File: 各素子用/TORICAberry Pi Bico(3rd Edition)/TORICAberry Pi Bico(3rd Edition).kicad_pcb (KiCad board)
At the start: 2 copper layers, 24.2 x 33.9 mm, 47 parts, among them J1 USB_C_Receptacle, J2 Conn_01x08_Socket, J5 Conn_01x11_Socket, SW1 SW_Push, SW2 SW_Push, U1 RP2040, U3 NCP1117-3.3_TO252, Y1 Crystal_GND24

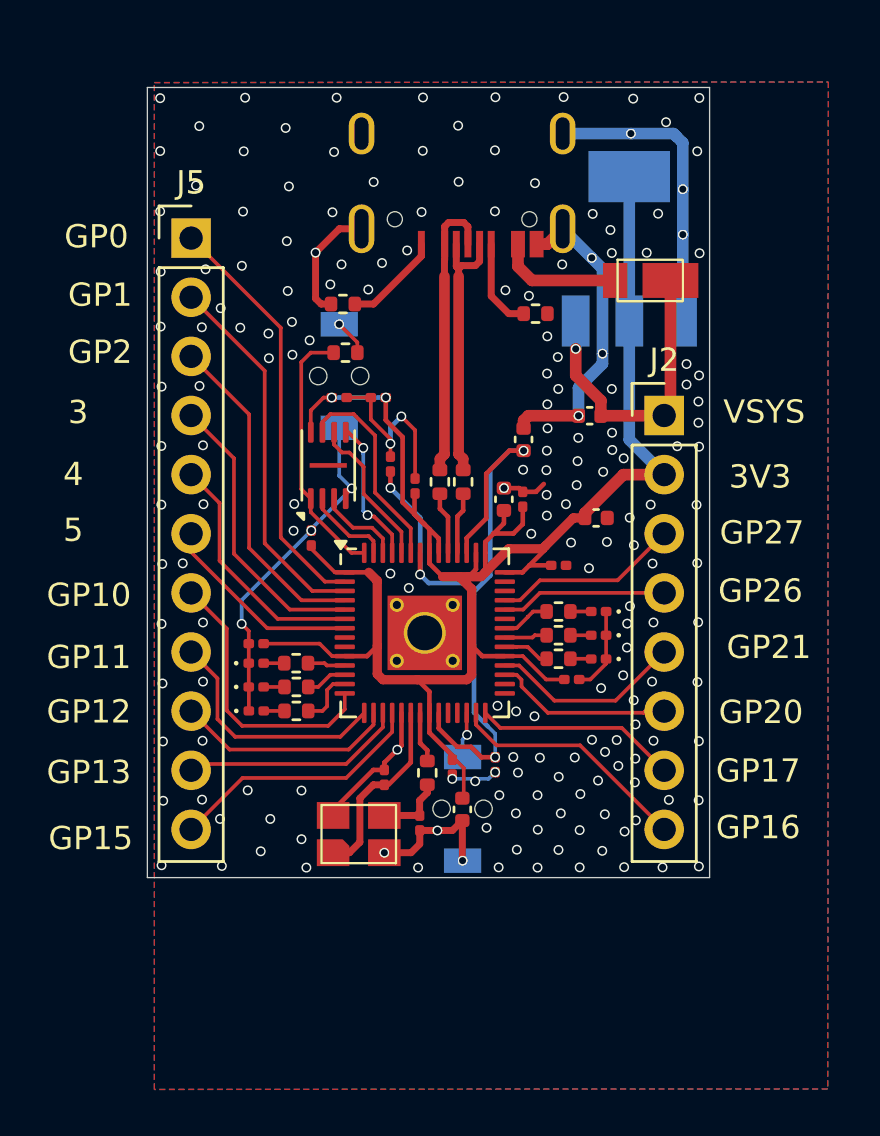
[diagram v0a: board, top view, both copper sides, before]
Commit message: RX-ESP delete
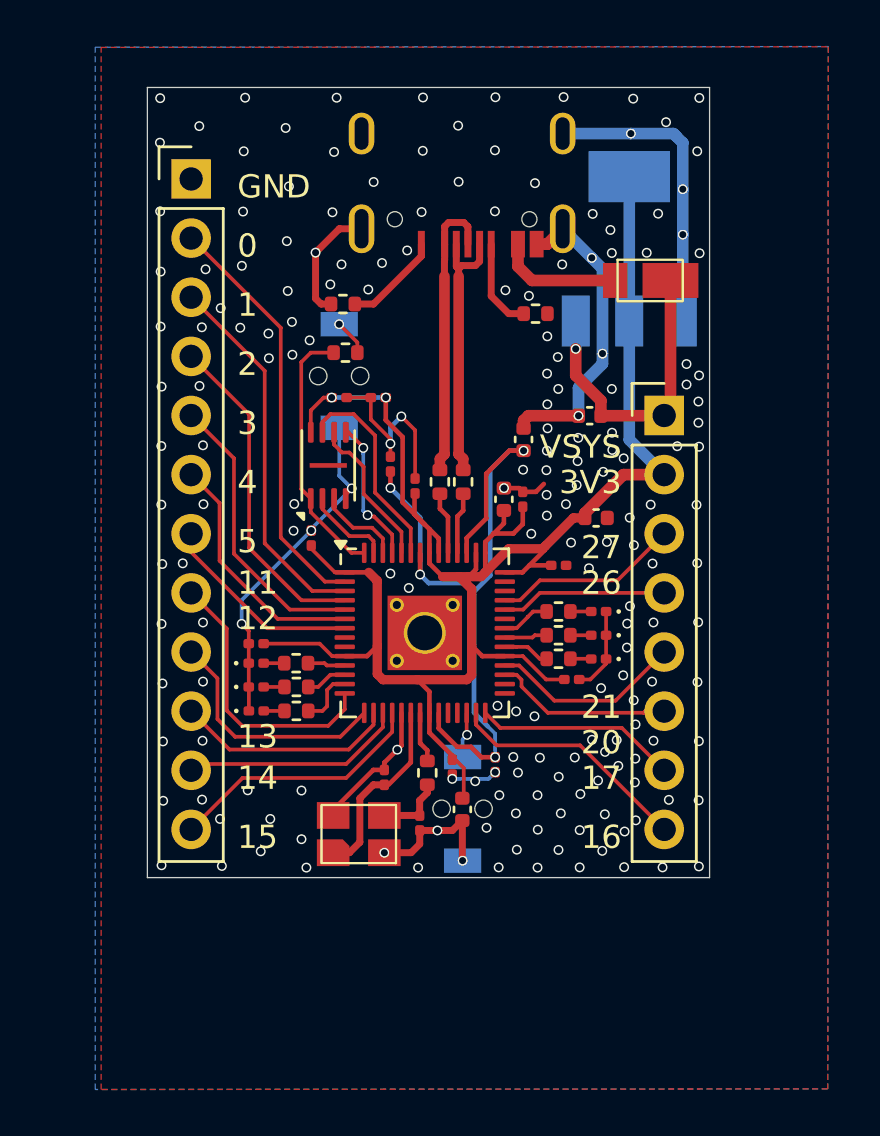
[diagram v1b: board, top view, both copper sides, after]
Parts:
- removed J5: Conn_01x11_Socket, Connector_PinHeader_2.54mm:PinHeader_1x11_P2.54mm_Vertical
- added J3: Conn_01x12_Socket, Connector_PinHeader_2.54mm:PinHeader_1x12_P2.54mm_Vertical, F.Cu at (100.4, 37.7)
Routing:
- net GND: vias 193 -> 192
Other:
- board text added: "0"
- board text added: "1"
- board text added: "11"
- board text added: "12"
- board text added: "13"
- board text added: "14"
- board text added: "15"
- board text added: "16"
- board text added: "17"
- board text added: "2"
- board text added: "20"
- board text added: "21"
- board text added: "26"
- board text added: "27"
- board text added: "GND"
- board text removed: "GP0"
- board text removed: "GP1"
- board text removed: "GP10"
- board text removed: "GP11"
- board text removed: "GP12"
- board text removed: "GP13"
- board text removed: "GP15"
- board text removed: "GP16"
- board text removed: "GP17"
- board text removed: "GP2"
- board text removed: "GP20"
- board text removed: "GP21"
- board text removed: "GP26"
- board text removed: "GP27"
